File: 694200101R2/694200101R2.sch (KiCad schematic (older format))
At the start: 265 parts, among them J1 USB4085-GF-A, J2 Conn_01x05_Male, J3 Conn_01x02_Male, SW1 MX_SW, SW10 MX_SW, SW100 MX_SW, SW101 MX_SW, SW102 MX_SW, SW103 MX_SW, SW104 MX_SW, SW105 MX_SW, SW106 MX_SW, SW107 MX_SW, SW11 MX_SW, SW12 MX_SW, SW13 MX_SW, SW14 MX_SW, SW15 MX_SW, SW16 MX_SW, SW17 MX_SW, SW18 MX_SW, SW19 MX_SW, SW2 MX_SW, SW20 MX_SW, SW21 MX_SW, SW22 MX_SW, SW23 MX_SW, SW24 MX_SW, SW25 MX_SW, SW26 MX_SW, SW27 MX_SW, SW28 MX_SW, SW29 MX_SW, SW3 MX_SW, SW30 MX_SW, SW31 MX_SW, SW32 MX_SW, SW33 MX_SW, SW34 MX_SW, SW35 MX_SW, SW36 MX_SW, SW37 MX_SW, SW38 MX_SW, SW39 MX_SW, SW4 MX_SW, SW40 MX_SW, SW41 MX_SW, SW42 MX_SW, SW43 MX_SW, SW44 MX_SW, SW45 MX_SW, SW46 MX_SW, SW47 MX_SW, SW48 MX_SW, SW49 MX_SW, SW5 MX_SW, SW50 MX_SW, SW51 MX_SW, SW52 MX_SW, SW53 MX_SW, SW54 MX_SW, SW55 MX_SW, SW56 MX_SW, SW57 MX_SW, SW58 MX_SW, SW59 MX_SW, SW6 MX_SW, SW60 MX_SW, SW61 MX_SW, SW62 MX_SW, SW63 MX_SW, SW64 MX_SW, SW65 MX_SW, SW66 MX_SW, SW67 MX_SW, SW68 MX_SW, SW69 MX_SW, SW7 MX_SW, SW70 MX_SW, SW71 MX_SW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

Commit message: created rev2 to work
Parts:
- removed J2: Conn_01x05_Male, Connector_PinHeader_2.54mm:PinHeader_1x05_P2.54mm_Vertical, symbol Connector:Conn_01x05_Male
- added J2: Conn_01x06_Male, symbol Connector:Conn_01x06_Male
- added R?: RNCP0603FTD10K0, Resistor-Libs:RESC1508X50N, symbol Resistor-Lib:RNCP0603FTD10K0
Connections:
- wire segments 660 -> 665
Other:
- moved on the sheet: C3, C6, J3, Y1

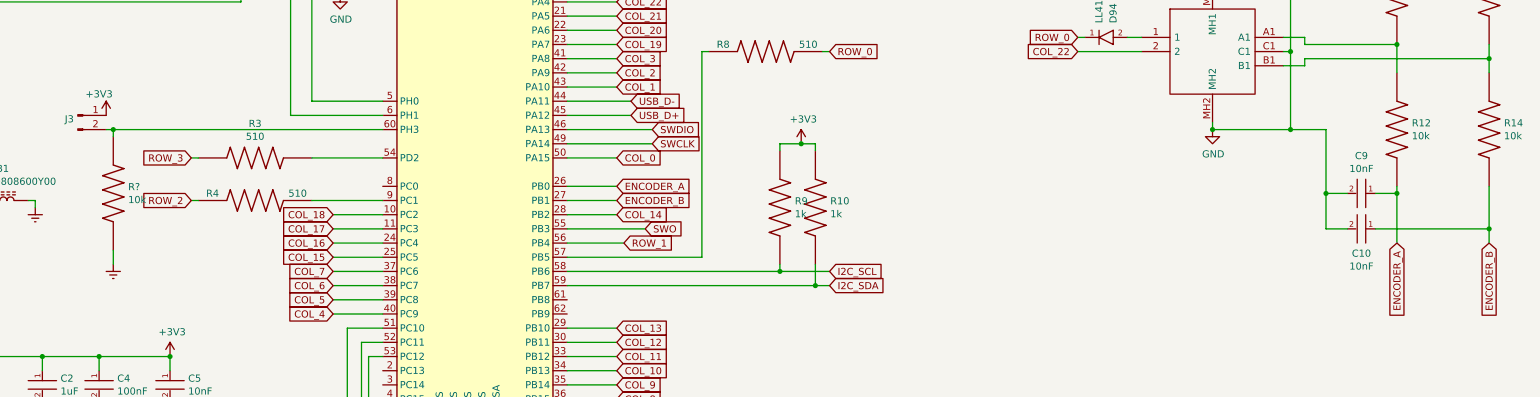
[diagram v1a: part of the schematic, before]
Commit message: adjusted led and added pull on program
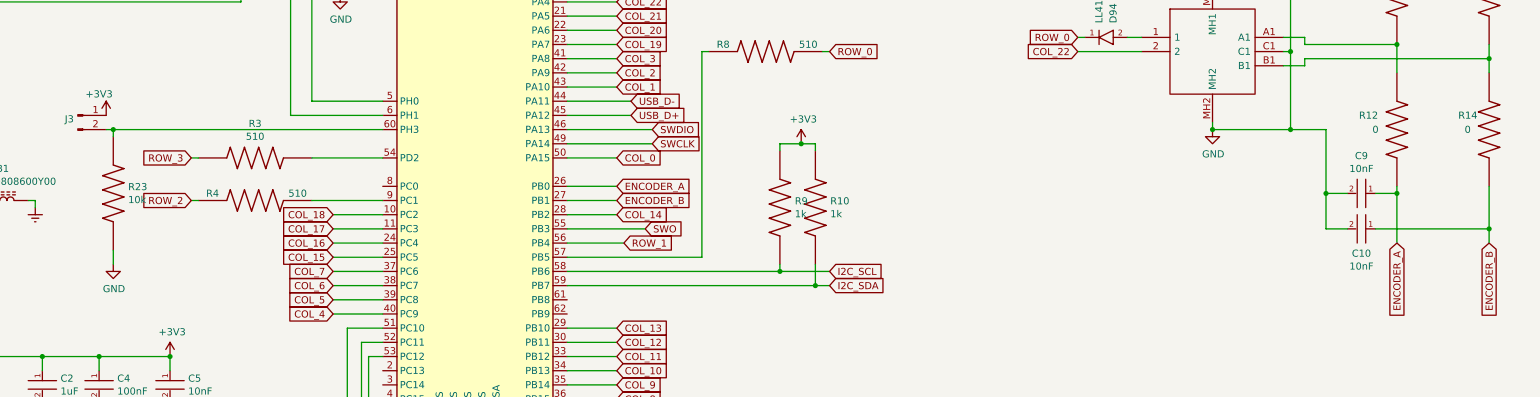
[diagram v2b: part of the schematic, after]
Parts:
- removed R12, R14, R?: RNCP0603FTD10K0, Resistor-Libs:RESC1508X50N, symbol Resistor-Lib:RNCP0603FTD10K0
- added R12, R14: MCT06030Z0000ZP500, Resistor-Libs:RESC1508X55N, symbol Resistor-Lib:MCT06030Z0000ZP500
- added R23: RNCP0603FTD10K0, Resistor-Libs:RESC1508X50N, symbol Resistor-Lib:RNCP0603FTD10K0
- J2: footprint (none) -> Connector_PinHeader_2.54mm:PinHeader_1x06_P2.54mm_Vertical
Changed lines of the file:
@@
 	15400 7300 15400 7500
 Connection ~ 15400 7300
-$Comp
-L Resistor-Lib:RNCP0603FTD10K0 R12
-U 1 1 5FF01719
-P 15400 7900
-F 0 "R12" V 15354 8005 50  0000 L CNN
-F 1 "RNCP0603FTD10K0" H 15100 7700 50  0001 L BNN
-F 2 "Resistor-Libs:RESC1508X50N" H 15400 7900 50  0001 L BNN
-F 3 "" H 15400 7900 50  0001 L BNN
-F 4 "10k" V 15445 8005 50  0000 L CNN "resistance"
-	1    15400 7900
-	0    1    1    0
-$EndComp
-$Comp
-L Resistor-Lib:RNCP0603FTD10K0 R14
-U 1 1 5FF03334
-P 16050 7900
-F 0 "R14" V 16004 8005 50  0000 L CNN
-F 1 "RNCP0603FTD10K0" H 15750 7700 50  0001 L BNN
-F 2 "Resistor-Libs:RESC1508X50N" H 16050 7900 50  0001 L BNN
-F 3 "" H 16050 7900 50  0001 L BNN
-F 4 "10k" V 16095 8005 50  0000 L CNN "resistance"
-	1    16050 7900
-	0    1    1    0
-$EndComp
 Wire Wire Line
 	16050 7400 16050 7500
@@
 Wire Wire Line
 	15400 8350 15400 8700
-Wire Wire Line
-	15250 8600 16050 8600
-Wire Wire Line
-	16050 8600 16050 8300
-Wire Wire Line
-	16050 8600 16050 8700
-Connection ~ 16050 8600
 Text GLabel 15400 8700 3    50   Input ~ 0
 ENCODER_A
-Text GLabel 16050 8700 3    50   Input ~ 0
-ENCODER_B
 Text GLabel 9900 8300 2    50   Input ~ 0
 ENCODER_A
@@
 Wire Wire Line
 	7050 6900 7050 6750
-$Comp
-L Resistor-Lib:RNCP0603FTD10K0 R?
-U 1 1 6188439F
-P 6350 8350
-F 0 "R?" V 6304 8455 50  0000 L CNN
-F 1 "RNCP0603FTD10K0" H 6050 8150 50  0001 L BNN
-F 2 "Resistor-Libs:RESC1508X50N" H 6350 8350 50  0001 L BNN
-F 3 "" H 6350 8350 50  0001 L BNN
-F 4 "10k" V 6395 8455 50  0000 L CNN "resistance"
-	1    6350 8350
-	0    1    1    0
-$EndComp
 Connection ~ 5350 6750
 Wire Wire Line
@@
 Wire Wire Line
 	6350 7900 8250 7900
-$Comp
-L power:Earth #PWR?
-U 1 1 620E18A5
-P 6350 8850
-F 0 "#PWR?" H 6350 8600 50  0001 C CNN
-F 1 "Earth" H 6350 8700 50  0001 C CNN
-F 2 "" H 6350 8850 50  0001 C CNN
-F 3 "~" H 6350 8850 50  0001 C CNN
-	1    6350 8850
-	1    0    0    -1
-$EndComp
 Wire Wire Line
 	6350 8750 6350 8850
@@
 F 0 "J2" H 7458 6231 50  0000 C CNN
 F 1 "Conn_01x06_Male" H 7458 6140 50  0000 C CNN
-F 2 "" H 7350 5850 50  0001 C CNN
+F 2 "Connector_PinHeader_2.54mm:PinHeader_1x06_P2.54mm_Vertical" H 7350 5850 50  0001 C CNN
 F 3 "~" H 7350 5850 50  0001 C CNN
 	1    7350 5850
@@
 Connection ~ 7950 6600
 $Comp
-L power:+3V3 #PWR?
+L power:+3V3 #PWR05
 U 1 1 62499D89
 P 7650 6200
-F 0 "#PWR?" H 7650 6050 50  0001 C CNN
+F 0 "#PWR05" H 7650 6050 50  0001 C CNN
 F 1 "+3V3" H 7665 6373 50  0000 C CNN
 F 2 "" H 7650 6200 50  0001 C CNN
@@
 Wire Wire Line
 	7950 6600 8250 6600
+Text GLabel 16050 8700 3    50   Input ~ 0
+ENCODER_B
+Connection ~ 16050 8600
+Wire Wire Line
+	16050 8600 16050 8700
+Wire Wire Line
+	16050 8600 16050 8300
+Wire Wire Line
+	15250 8600 16050 8600
+$Comp
+L Resistor-Lib:MCT06030Z0000ZP500 R12
+U 1 1 62612D6A
+P 15400 7900
+F 0 "R12" V 15500 8100 50  0000 C CNN
+F 1 "MCT06030Z0000ZP500" H 15100 7700 50  0001 L BNN
+F 2 "Resistor-Libs:RESC1508X55N" H 15400 7900 50  0001 L BNN
+F 3 "" H 15400 7900 50  0001 L BNN
+F 4 "0" V 15400 8051 50  0000 C CNN "resistance"
+	1    15400 7900
+	0    -1   -1   0
+$EndComp
+$Comp
+L Resistor-Lib:MCT06030Z0000ZP500 R14
+U 1 1 6259D68A
+P 16050 7900
+F 0 "R14" V 16150 8050 50  0000 C CNN
+F 1 "MCT06030Z0000ZP500" H 15750 7700 50  0001 L BNN
+F 2 "Resistor-Libs:RESC1508X55N" H 16050 7900 50  0001 L BNN
+F 3 "" H 16050 7900 50  0001 L BNN
+F 4 "0" V 16050 8051 50  0000 C CNN "resistance"
+	1    16050 7900
+	0    -1   -1   0
+$EndComp
+$Comp
+L Resistor-Lib:RNCP0603FTD10K0 R23
+U 1 1 62F6D73A
+P 6350 8350
+F 0 "R23" V 6304 8455 50  0000 L CNN
+F 1 "RNCP0603FTD10K0" H 6050 8150 50  0001 L BNN
+F 2 "Resistor-Libs:RESC1508X50N" H 6350 8350 50  0001 L BNN
+F 3 "" H 6350 8350 50  0001 L BNN
+F 4 "10k" V 6395 8455 50  0000 L CNN "resistance"
+	1    6350 8350
+	0    1    1    0
+$EndComp
+$Comp
+L power:GND #PWR?
+U 1 1 63063077
+P 6350 8850
+F 0 "#PWR?" H 6350 8600 50  0001 C CNN
+F 1 "GND" H 6355 8677 50  0000 C CNN
+F 2 "" H 6350 8850 50  0001 C CNN
+F 3 "" H 6350 8850 50  0001 C CNN
+	1    6350 8850
+	1    0    0    -1
+$EndComp
 $EndSCHEMATC

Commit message: Added Logo and updated USB Connector
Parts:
- removed G1: LOGO, BossLogo:BossLogo, symbol 694200101-rescue:LOGO-BossLogo
- removed J1: USB4085-GF-A, Connector_USB:USB_C_Receptacle_GCT_USB4085, symbol eec-gct:USB4085-GF-A
- added J1: USB_C_Receptacle_USB2.0, Connector_USB:USB_C_Receptacle_GCT_USB4085, symbol Connector:USB_C_Receptacle_USB2.0
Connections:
- wire segments 665 -> 653
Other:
- moved on the sheet: C1, R1, R2, R21, R22, U2

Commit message: Prettied up schematic
Updated Schematic to be more readable and not as crazily wired
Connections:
- net +3V3: now also U1.3 (VOUT)
- net GND: now also U1.2 (GND), U1.4 (EPAD), Y1.4 (GND)
- net VCC: now also U1.1 (VIN)
- net OSC_IN: now reaches C6.1, U3.5 (PH0)
- net OSC_IN: now also Y1.3 (OUT/IN)
- net ROW_6_MCU: now reaches R5.2, U3.51 (PC10)
- net ROW_5_MCU: now reaches R6.2, U3.52 (PC11)
- net ROW_4_MCU: now reaches R7.2, U3.53 (PC12)
- net ROW_3_MCU: now reaches R3.2, U3.54 (PD2)
- net ROW_0_MCU: now reaches R8.1, U3.57 (PB5)
- net OSC_OUT: now reaches C3.1, U3.6 (PH1), Y1.1 (IN/OUT)
- net BOOT0: now reaches J3.2 (Pin_2), R23.1, U3.60 (PH3)
- net ROW_2_MCU: now reaches R4.2, U3.9 (PC1)
- no-connect marks 0 -> 2
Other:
- note added: "BOOT0 Set"
- note added: "I2C Pull-Up Resistors"
- note added: "JTAG/RST"
- note added: "LDO 5V to 3V3 Dropdown"
- note added: "MCU Oscillator"
- note added: "Matrix Current Limiting Resistors"
- note added: "Stabs and Mounting Holes"
- note added: "USB C Connector with Protection"
- moved on the sheet: C1, C2, C25, C3, C4, C5, C6, C7, C8, CR1, F1, FB1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

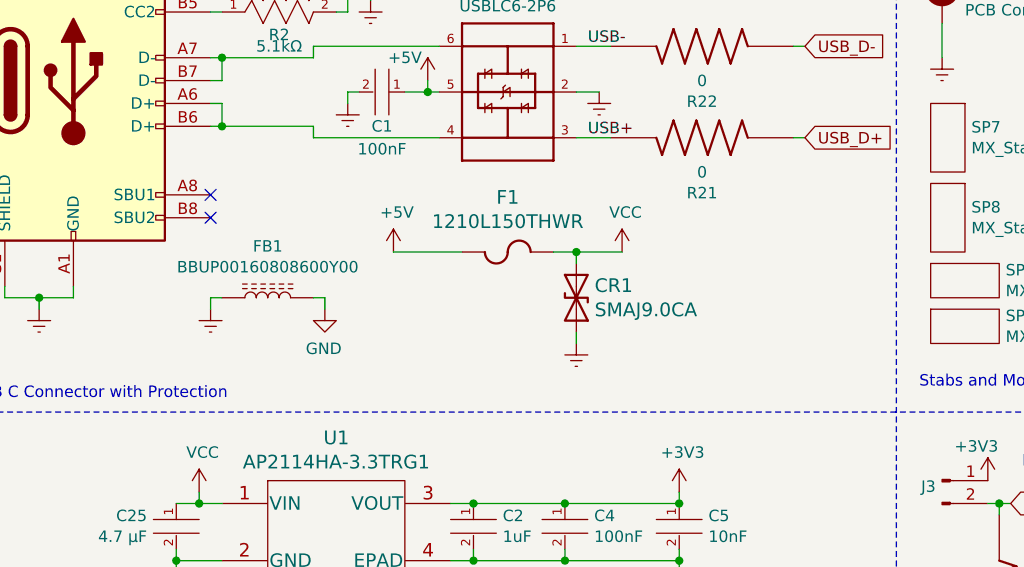
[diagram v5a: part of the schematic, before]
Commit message: fixed protection schematic
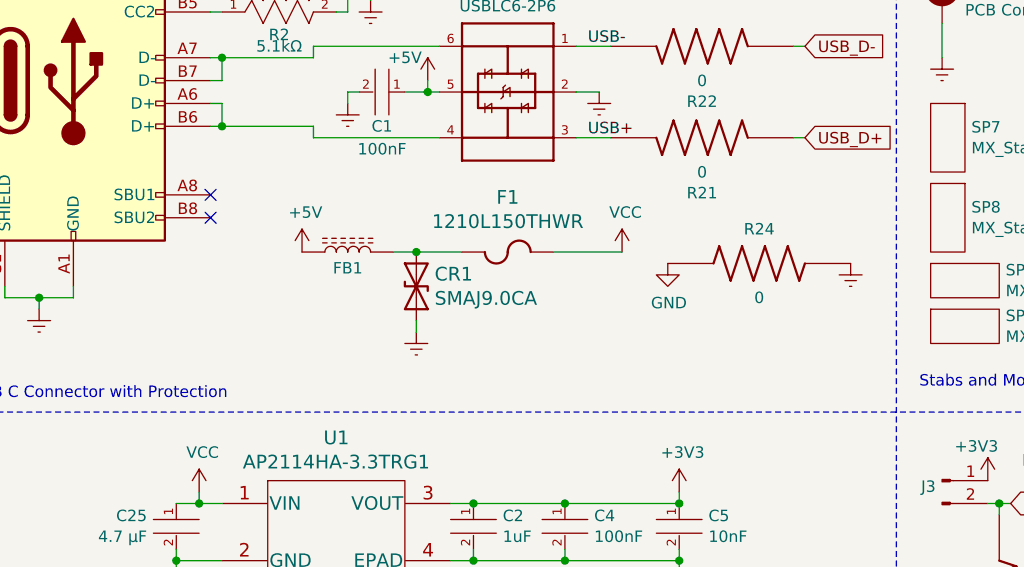
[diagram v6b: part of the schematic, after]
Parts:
- added R24: MCT06030Z0000ZP500, Resistor-Libs:RESC1508X55N, symbol Resistor-Lib:MCT06030Z0000ZP500
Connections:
- net +5V: now also FB1.2; no longer F1.1
- net Earth: now also R24.1; no longer FB1.2
- net GND: now also R24.2; no longer FB1.1
- net VCC: no longer CR1.1 (A1)
- new net: CR1.1 (A1), F1.1, FB1.1
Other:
- moved on the sheet: CR1, FB1
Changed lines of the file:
@@
 $EndComp
-$Comp
-L power:GND #PWR0107
-U 1 1 607B8F03
-P 2250 6950
-F 0 "#PWR0107" H 2250 6700 50  0001 C CNN
-F 1 "GND" H 2255 6777 50  0000 C CNN
-F 2 "" H 2250 6950 50  0001 C CNN
-F 3 "" H 2250 6950 50  0001 C CNN
-	1    2250 6950
-	-1   0    0    -1
-$EndComp
-$Comp
-L power:Earth #PWR0108
-U 1 1 607C0525
-P 1750 6950
-F 0 "#PWR0108" H 1750 6700 50  0001 C CNN
-F 1 "Earth" H 1750 6800 50  0001 C CNN
-F 2 "" H 1750 6950 50  0001 C CNN
-F 3 "~" H 1750 6950 50  0001 C CNN
-	1    1750 6950
-	-1   0    0    -1
-$EndComp
-Wire Wire Line
-	2250 6900 2250 6950
 $Comp
 L power:GND #PWR0109
@@
 	1    0    0    -1
 $EndComp
-Wire Wire Line
-	2250 6900 2200 6900
-Wire Wire Line
-	1800 6900 1750 6900
-Wire Wire Line
-	1750 6900 1750 6950
 $Comp
 L cldg:BBUP00160808600Y00 FB1
 U 1 1 604967EC
-P 1950 7000
-F 0 "FB1" H 1900 7325 50  0000 C CNN
-F 1 "BBUP00160808600Y00" H 1900 7234 50  0000 C CNN
-F 2 "Resistor-Libs:Yageo-RC0603-0-0-IPC_C" H 1950 7000 50  0001 C CNN
-F 3 "" H 1950 7000 50  0001 C CNN
-	1    1950 7000
+P 2300 6800
+F 0 "FB1" H 2250 6800 50  0000 C BNN
+F 1 "BBUP00160808600Y00" H 2250 7034 50  0001 C CNN
+F 2 "Resistor-Libs:Yageo-RC0603-0-0-IPC_C" H 2300 6800 50  0001 C CNN
+F 3 "" H 2300 6800 50  0001 C CNN
+	1    2300 6800
 	-1   0    0    -1
 $EndComp
@@
 L power:+5V #PWR03
 U 1 1 5FFA23B6
-P 2550 6700
-F 0 "#PWR03" H 2550 6550 50  0001 C CNN
-F 1 "+5V" H 2565 6873 50  0000 C CNN
-F 2 "" H 2550 6700 50  0001 C CNN
-F 3 "" H 2550 6700 50  0001 C CNN
-	1    2550 6700
+P 2150 6700
+F 0 "#PWR03" H 2150 6550 50  0001 C CNN
+F 1 "+5V" H 2165 6873 50  0000 C CNN
+F 2 "" H 2150 6700 50  0001 C CNN
+F 3 "" H 2150 6700 50  0001 C CNN
+	1    2150 6700
 	1    0    0    -1
 $EndComp
@@
 $EndComp
 Wire Wire Line
-	2550 6700 2850 6700
-Wire Wire Line
-	3250 6700 3350 6700
-Wire Wire Line
-	3350 6700 3350 6750
-Connection ~ 3350 6700
+	2550 6700 2650 6700
 $Comp
 L power:VCC #PWR0101
@@
 	1    0    0    -1
 $EndComp
-Wire Wire Line
-	3350 6700 3550 6700
 $Comp
 L Littlefuse:SMAJ9.0CA CR1
 U 1 1 60252249
-P 3300 6700
-F 0 "CR1" V 3447 6830 60  0000 L CNN
-F 1 "SMAJ9.0CA" V 3553 6830 60  0000 L CNN
-F 2 "Littlefuse:SMAJ9.0CA" H 3500 6540 60  0001 C CNN
-F 3 "" H 3300 6700 60  0000 C CNN
-	1    3300 6700
+P 2600 6650
+F 0 "CR1" V 2747 6780 60  0000 L CNN
+F 1 "SMAJ9.0CA" V 2853 6780 60  0000 L CNN
+F 2 "Littlefuse:SMAJ9.0CA" H 2800 6490 60  0001 C CNN
+F 3 "" H 2600 6650 60  0000 C CNN
+	1    2600 6650
 	0    1    1    0
 $EndComp
 Wire Wire Line
-	3350 7050 3350 7100
+	2650 7000 2650 7050
 $Comp
 L power:Earth #PWR0104
 U 1 1 60423113
-P 3350 7100
-F 0 "#PWR0104" H 3350 6850 50  0001 C CNN
-F 1 "Earth" H 3350 6950 50  0001 C CNN
-F 2 "" H 3350 7100 50  0001 C CNN
-F 3 "~" H 3350 7100 50  0001 C CNN
-	1    3350 7100
+P 2650 7050
+F 0 "#PWR0104" H 2650 6800 50  0001 C CNN
+F 1 "Earth" H 2650 6900 50  0001 C CNN
+F 2 "" H 2650 7050 50  0001 C CNN
+F 3 "~" H 2650 7050 50  0001 C CNN
+	1    2650 7050
 	1    0    0    -1
 $EndComp
@@
 Wire Notes Line
 	650  7400 8650 7400
+Wire Wire Line
+	3250 6700 3550 6700
+Connection ~ 2650 6700
+Wire Wire Line
+	2650 6700 2850 6700
+$Comp
+L power:GND #PWR02
+U 1 1 62F09F65
+P 3750 6750
+F 0 "#PWR02" H 3750 6500 50  0001 C CNN
+F 1 "GND" H 3755 6577 50  0000 C CNN
+F 2 "" H 3750 6750 50  0001 C CNN
+F 3 "" H 3750 6750 50  0001 C CNN
+	1    3750 6750
+	1    0    0    -1
+$EndComp
+$Comp
+L power:Earth #PWR031
+U 1 1 62F79601
+P 4550 6750
+F 0 "#PWR031" H 4550 6500 50  0001 C CNN
+F 1 "Earth" H 4550 6600 50  0001 C CNN
+F 2 "" H 4550 6750 50  0001 C CNN
+F 3 "~" H 4550 6750 50  0001 C CNN
+	1    4550 6750
+	1    0    0    -1
+$EndComp
+$Comp
+L Resistor-Lib:MCT06030Z0000ZP500 R24
+U 1 1 62FE7825
+P 4150 6750
+F 0 "R24" H 4150 6600 50  0000 C CNN
+F 1 "MCT06030Z0000ZP500" H 3850 6550 50  0001 L BNN
+F 2 "Resistor-Libs:RESC1508X55N" H 4150 6750 50  0001 L BNN
+F 3 "" H 4150 6750 50  0001 L BNN
+F 4 "0" H 4150 6900 50  0000 C CNN "resistance"
+	1    4150 6750
+	-1   0    0    1
+$EndComp
 $EndSCHEMATC

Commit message: Updated Footprints and Fixed Schematic Warnings
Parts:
- removed C10, C5, C9: CL10B103KB8NNNC, capacitor-lib:Samsung-0603_1608_Metric-0-0-0, symbol capacitor-lib:CL10B103KB8NNNC
- removed C2: CL10B105KA8NNNC, capacitor-lib:Samsung-CL10-0-0-IPC_C, symbol capacitor-lib:CL10B105KA8NNNC
- removed C25: CL21A475KAQNNNE, Capacitor_SMD:C_0805_2012Metric, symbol capacitor-lib:CL21A475KAQNNNE
- removed C4, C8: CL10B104KB8NNNL, capacitor-lib:Samsung-CL10-09_2006-0-IPC_C, symbol capacitor-lib:CL10B104KB8NNNL
- removed D1, D14, D20, D25, D35, D40, D45, D50, D56, D62, D66, D71, D75, D79, D9: LL4148, Diode_SMD:D_MiniMELF, symbol eec-fairchild:LL4148
- removed ENC1: PEC11L-4115F-S0020, PEC11L4115FS0020, symbol SamacSys_Parts:PEC11L-4115F-S0020
- removed F1: 1210L150THWR, Fuse:Fuse_1210_3225Metric, symbol Littlefuse:1210L150THWR
- removed R11, R13: RNCP0603FTD10K0, Resistor-Libs:RESC1508X50N, symbol Resistor-Lib:RNCP0603FTD10K0
- removed R12, R14: MCT06030Z0000ZP500, Resistor-Libs:RESC1508X55N, symbol Resistor-Lib:MCT06030Z0000ZP500
- removed U1: AP2114HA-3.3TRG1, DI-LVO:AP2114HA-3.3TRG1, symbol DI-LVO:AP2114HA-3.3TRG1
- removed U2: USBLC6-2P6, SOT50P160X60-6N, symbol cldg:USBLC6-2P6
- added C10, C5, C9: 10nF, Capacitor_SMD:C_0603_1608Metric, symbol Device:C
- added C2: 1uF, Capacitor_SMD:C_0603_1608Metric, symbol Device:C
- added C25: 4.7 uF, Capacitor_SMD:C_0805_2012Metric, symbol Device:C
- added C4, C8: 100nF, Capacitor_SMD:C_0603_1608Metric, symbol Device:C
- added D1, D14, D20, D25, D35, D40, D45, D50, D56, D62, D66, D71, D75, D79, D9: LL4148, Diode_SMD:D_MiniMELF, symbol Diode:LL4148
- added ENC1: PEC11R-4215F-S0024, digikey-footprints:Rotary_Encoder_Switched_PEC11R, symbol cldg:PEC11R-4215F-S0024
- added F1: 1210L150THWR, Fuse:Fuse_1210_3225Metric_Castellated, symbol Device:Polyfuse
- added U1: AP2114HA-3_3TRG1, digikey-footprints:SOT-223, symbol cldg:AP2114HA-3_3TRG1
- added U2: USBLC6-2P6, Package_TO_SOT_SMD:SOT-666, symbol Power_Protection:USBLC6-2P6
- C1, C7: footprint capacitor-lib:Samsung-CL10-09_2006-0-IPC_C -> Capacitor_SMD:C_0603_1608Metric
- C3, C6: footprint capacitor-lib:AVX-GRM124-0-0-IPC_C -> Capacitor_SMD:C_0603_1608Metric
- D10, D100, D101, D102, D103, D104, D105, D106, D107, D108, D11, D12, D13, D15, D16, D17, D18, D19, D2, D21, D22, D23, D24, D26, D27, D28, D29, D3, D30, D31, D32, D33, D34, D36, D37, D38, D39, D4, D41, D42, D43, D44, D46, D47, D48, D49, D5, D51, D52, D53, D54, D55, D57, D58, D59, D6, D60, D61, D63, D64, D65, D67, D68, D69, D7, D70, D72, D73, D74, D76, D77, D78, D8, D80, D81, D82, D83, D84, D85, D86, D87, D88, D89, D90, D91, D92, D93, D94, D95, D96, D97, D98, D99: symbol eec-fairchild:LL4148 -> Diode:LL4148
- FB1, R1, R2: footprint Resistor-Libs:Yageo-RC0603-0-0-IPC_C -> Resistor_SMD:R_0603_1608Metric
- R10, R21, R22, R24, R9: footprint Resistor-Libs:RESC1508X55N -> Resistor_SMD:R_0603_1608Metric
- R23: footprint Resistor-Libs:RESC1508X50N -> Resistor_SMD:R_0603_1608Metric
- R3, R4, R5, R6, R7, R8: footprint Resistor-Libs:RESC2012X65N -> Resistor_SMD:R_0805_2012Metric
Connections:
- net +3V3: now also C2.1, C4.1, C5.1, C8.1, U1.2 (VOUT)
- net +5V: now also U2.5 (VBUS)
- net COL_22: now also ENC1.2
- net ENCODER_A: now also C10.1, ENC1.A (CH_A)
- net ENCODER_B: now also C9.1, ENC1.B (CH_B)
- net Earth: now also U2.2 (GND)
- net GND: now also C10.2, C2.2, C25.2, C4.2, C5.2, C9.2, ENC1.3, ENC1.C (COM), U1.1 (GND), U1.4 (GND)
- net ROW_0: now also D1.1 (K), D14.1 (K), D20.1 (K), D25.1 (K), D35.1 (K), D40.1 (K), D45.1 (K), D50.1 (K), D56.1 (K), D62.1 (K), D66.1 (K), D71.1 (K), D75.1 (K), D79.1 (K), D9.1 (K)
- net USB+: now also U2.3 (I/O2)
- net USB-: now also U2.1 (I/O1)
- net VCC: now also C25.1, F1.1, U1.3 (IN)
- net at U3.1 (VBAT): now also C8.2
- net at D94.2 (A): now also ENC1.1
- net at J1.A6 (D+), J1.B6 (D+): now also U2.4 (I/O2)
- net at J1.A7 (D-), J1.B7 (D-): now also U2.6 (I/O1)
- net at CR1.1 (A1), FB1.1: now also F1.2
- net at SW40.1: now also D40.2 (A)
- net at SW1.1: now also D1.2 (A)
- net at SW9.1: now also D9.2 (A)
- net at SW14.1: now also D14.2 (A)
- net at SW20.1: now also D20.2 (A)
- net at SW25.1: now also D25.2 (A)
- net at SW35.1: now also D35.2 (A)
- net at SW45.1: now also D45.2 (A)
- net at SW50.1: now also D50.2 (A)
- net at SW56.1: now also D56.2 (A)
- net at SW62.1: now also D62.2 (A)
- net at SW66.1: now also D66.2 (A)
- net at SW71.1: now also D71.2 (A)
- net at SW75.1: now also D75.2 (A)
- net at SW79.1: now also D79.2 (A)
- net COL_18: no longer names the net of U3.10 (PC2)
- net ROW_1: no longer names the net of U3.56 (PB4)
- no-connect marks 2 -> 14
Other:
- note added: "Debug and boot-set headers"
- note added: "Encoder"
- moved on the sheet: C1, C3, C6, CR1, FB1, R24, U3, Y1

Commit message: Updated Schematic
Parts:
- removed R24: MCT06030Z0000ZP500, Resistor_SMD:R_0603_1608Metric, symbol Resistor-Lib:MCT06030Z0000ZP500
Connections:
- net Earth: now also FB1.1
- net GND: now also FB1.2
- net VCC: now also CR1.1 (A1)
- net +5V renamed VBUS
- net VBUS: now also F1.2; no longer FB1.2
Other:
- moved on the sheet: C10, C8, C9, CR1, D94, ENC1, F1, FB1, U3
